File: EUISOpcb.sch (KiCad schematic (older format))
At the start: 13 parts

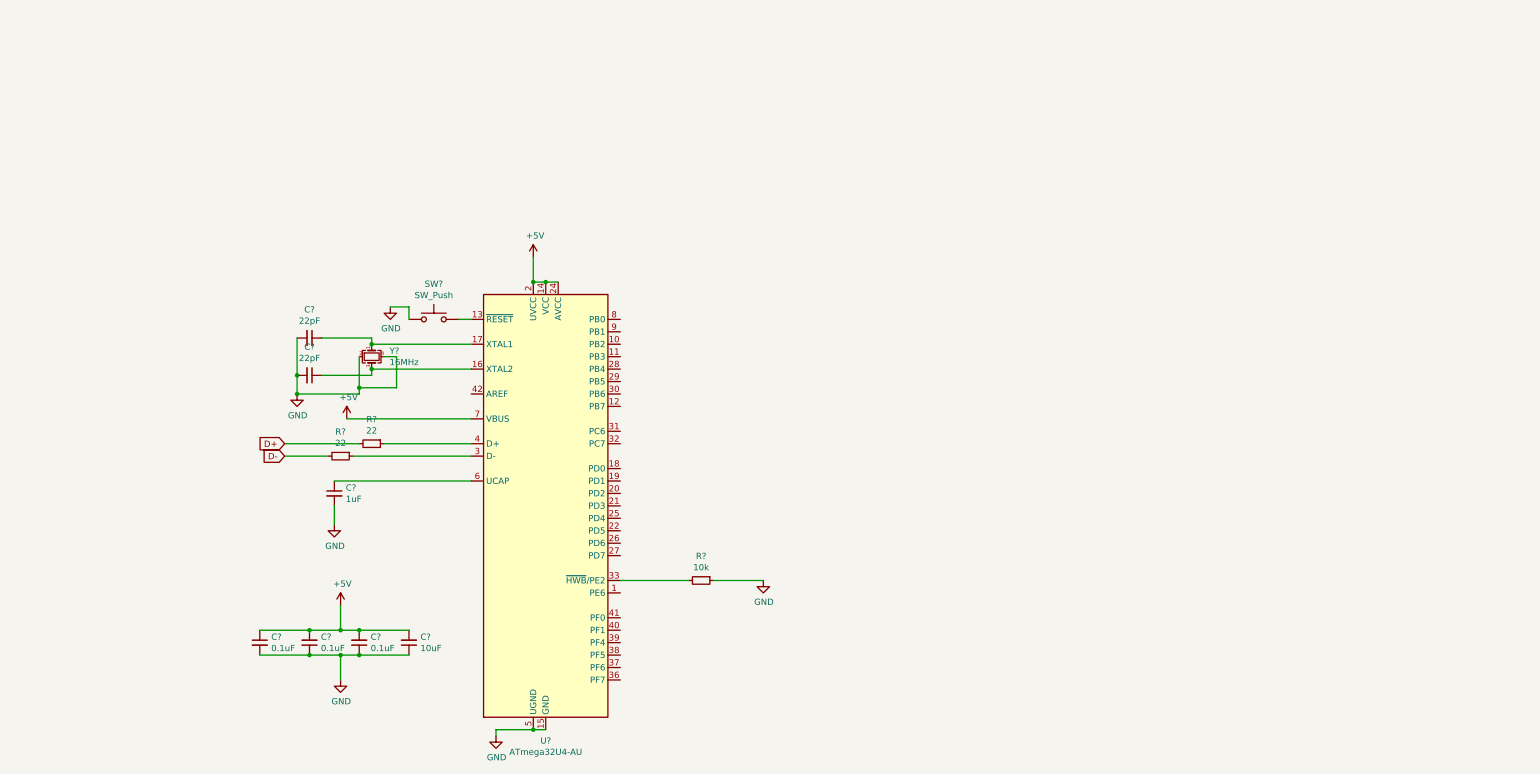
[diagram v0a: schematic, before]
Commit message: PCB Schematic/Traces Complete
Completed the PCB Schematic and traces!
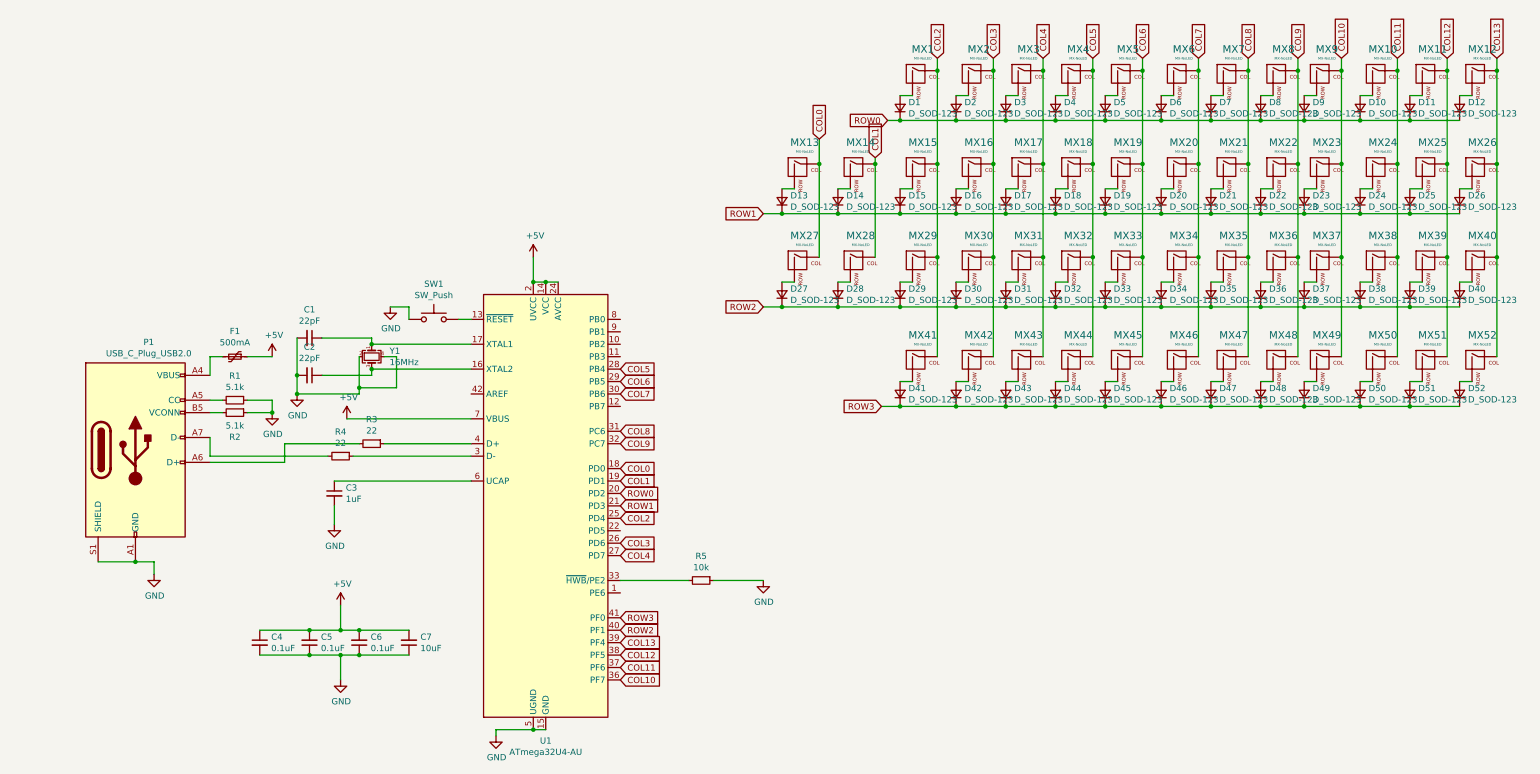
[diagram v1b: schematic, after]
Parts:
- added D1, D10, D11, D12, D13, D14, D15, D16, D17, D18, D19, D2, D20, D21, D22, D23, D24, D25, D26, D27, D28, D29, D3, D30, D31, D32, D33, D34, D35, D36, D37, D38, D39, D4, D40, D41, D42, D43, D44, D45, D46, D47, D48, D49, D5, D50, D51, D52, D6, D7, D8, D9: D_SOD-123, Diode_SMD:D_SOD-123, symbol Device:D_Small
- added F1: 500mA, Fuse:Fuse_1206_3216Metric, symbol Device:Polyfuse_Small
- added MX1, MX10, MX11, MX12, MX15, MX16, MX17, MX18, MX19, MX2, MX20, MX21, MX22, MX23, MX24, MX25, MX26, MX29, MX3, MX30, MX31, MX32, MX33, MX34, MX35, MX36, MX37, MX38, MX39, MX4, MX40, MX41, MX42, MX43, MX44, MX45, MX46, MX47, MX48, MX49, MX5, MX50, MX51, MX52, MX6, MX7, MX8, MX9: MX-NoLED, MX_Only:MXOnly-1U-NoLED, symbol MX_Alps_Hybrid:MX-NoLED
- added MX13, MX14, MX27, MX28: MX-NoLED, MX_Only:MXOnly-ISO, symbol MX_Alps_Hybrid:MX-NoLED
- added P1: USB_C_Plug_USB2.0, Connector_USB:USB_C_Receptacle_Amphenol_12401548E4-2A, symbol Connector:USB_C_Plug_USB2.0
- added R1, R2: 5.1k, Resistor_SMD:R_0805_2012Metric, symbol Device:R_Small
- C1, C2, C3, C4, C5, C6, C7: renamed from C?; footprint (none) -> Capacitor_SMD:C_0805_2012Metric
- R3, R4, R5: renamed from R?; footprint (none) -> Resistor_SMD:R_0805_2012Metric
- SW1: renamed from SW?; footprint (none) -> random-keyboard-parts:SKQG-1155865
- Y1: renamed from Y?; footprint (none) -> Crystal:Crystal_SMD_3225-4Pin_3.2x2.5mm
- gave numbers to parts that had none: 1
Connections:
- net +5V: now also F1.1
- net GND: now also P1.A1 (GND), P1.A12 (GND), P1.B1 (GND), P1.B12 (GND), P1.S1 (SHIELD), R1.1, R2.1
- net COL0: now reaches U1.18 (PD0)
- net COL0: now also MX13.1 (COL), MX27.1 (COL)
- net COL1: now reaches U1.19 (PD1)
- net COL1: now also MX14.1 (COL), MX28.1 (COL)
- net ROW0: now reaches U1.20 (PD2)
- net ROW0: now also D1.1 (K), D10.1 (K), D11.1 (K), D12.1 (K), D2.1 (K), D3.1 (K), D4.1 (K), D5.1 (K), D6.1 (K), D7.1 (K), D8.1 (K), D9.1 (K)
- net ROW1: now reaches U1.21 (PD3)
- net ROW1: now also D13.1 (K), D14.1 (K), D15.1 (K), D16.1 (K), D17.1 (K), D18.1 (K), D19.1 (K), D20.1 (K), D21.1 (K), D22.1 (K), D23.1 (K), D24.1 (K), D25.1 (K), D26.1 (K)
- net COL2: now reaches U1.25 (PD4)
- net COL2: now also MX1.1 (COL), MX15.1 (COL), MX29.1 (COL), MX41.1 (COL)
- net COL3: now reaches U1.26 (PD6)
- net COL3: now also MX16.1 (COL), MX2.1 (COL), MX30.1 (COL), MX42.1 (COL)
- net COL4: now reaches U1.27 (PD7)
- net COL4: now also MX17.1 (COL), MX3.1 (COL), MX31.1 (COL), MX43.1 (COL)
- net COL5: now reaches U1.28 (PB4)
- net COL5: now also MX18.1 (COL), MX32.1 (COL), MX4.1 (COL), MX44.1 (COL)
- net COL6: now reaches U1.29 (PB5)
- net COL6: now also MX19.1 (COL), MX33.1 (COL), MX45.1 (COL), MX5.1 (COL)
- net COL7: now reaches U1.30 (PB6)
- net COL7: now also MX20.1 (COL), MX34.1 (COL), MX46.1 (COL), MX6.1 (COL)
- net COL8: now reaches U1.31 (PC6)
- net COL8: now also MX21.1 (COL), MX35.1 (COL), MX47.1 (COL), MX7.1 (COL)
- net COL9: now reaches U1.32 (PC7)
- net COL9: now also MX22.1 (COL), MX36.1 (COL), MX48.1 (COL), MX8.1 (COL)
- net COL10: now reaches U1.36 (PF7)
- net COL10: now also MX23.1 (COL), MX37.1 (COL), MX49.1 (COL), MX9.1 (COL)
- net COL11: now reaches U1.37 (PF6)
- net COL11: now also MX10.1 (COL), MX24.1 (COL), MX38.1 (COL), MX50.1 (COL)
- net COL12: now reaches U1.38 (PF5)
- net COL12: now also MX11.1 (COL), MX25.1 (COL), MX39.1 (COL), MX51.1 (COL)
- net COL13: now reaches U1.39 (PF4)
- net COL13: now also MX12.1 (COL), MX26.1 (COL), MX40.1 (COL), MX52.1 (COL)
- net ROW2: now reaches U1.40 (PF1)
- net ROW2: now also D27.1 (K), D28.1 (K), D29.1 (K), D30.1 (K), D31.1 (K), D32.1 (K), D33.1 (K), D34.1 (K), D35.1 (K), D36.1 (K), D37.1 (K), D38.1 (K), D39.1 (K), D40.1 (K)
- net ROW3: now reaches U1.41 (PF0)
- net ROW3: now also D41.1 (K), D42.1 (K), D43.1 (K), D44.1 (K), D45.1 (K), D46.1 (K), D47.1 (K), D48.1 (K), D49.1 (K), D50.1 (K), D51.1 (K), D52.1 (K)
- net D+: no longer names the net of R3.2
- net D+: now also P1.A6 (D+)
- net D-: no longer names the net of R4.2
- net D-: now also P1.A7 (D-)
- new net: F1.2, P1.A4 (VBUS), P1.A9 (VBUS), P1.B4 (VBUS), P1.B9 (VBUS)
- new net: P1.A5 (CC), R1.2
- new net: P1.B5 (VCONN), R2.2
- new net: D1.2 (A), MX1.2 (ROW)
- new net: D2.2 (A), MX2.2 (ROW)
- new net: D3.2 (A), MX3.2 (ROW)
- new net: D4.2 (A), MX4.2 (ROW)
- new net: D5.2 (A), MX5.2 (ROW)
- new net: D6.2 (A), MX6.2 (ROW)
- new net: D7.2 (A), MX7.2 (ROW)
- new net: D8.2 (A), MX8.2 (ROW)
- new net: D9.2 (A), MX9.2 (ROW)
- new net: D10.2 (A), MX10.2 (ROW)
- new net: D11.2 (A), MX11.2 (ROW)
- new net: D12.2 (A), MX12.2 (ROW)
- new net: D15.2 (A), MX15.2 (ROW)
- new net: D16.2 (A), MX16.2 (ROW)
- new net: D17.2 (A), MX17.2 (ROW)
- new net: D18.2 (A), MX18.2 (ROW)
- new net: D19.2 (A), MX19.2 (ROW)
- new net: D20.2 (A), MX20.2 (ROW)
- new net: D21.2 (A), MX21.2 (ROW)
- new net: D22.2 (A), MX22.2 (ROW)
- new net: D23.2 (A), MX23.2 (ROW)
- new net: D24.2 (A), MX24.2 (ROW)
- new net: D25.2 (A), MX25.2 (ROW)
- new net: D26.2 (A), MX26.2 (ROW)
- new net: D29.2 (A), MX29.2 (ROW)
- new net: D30.2 (A), MX30.2 (ROW)
- new net: D31.2 (A), MX31.2 (ROW)
- new net: D32.2 (A), MX32.2 (ROW)
- new net: D33.2 (A), MX33.2 (ROW)
- new net: D34.2 (A), MX34.2 (ROW)
- new net: D35.2 (A), MX35.2 (ROW)
- new net: D36.2 (A), MX36.2 (ROW)
- new net: D37.2 (A), MX37.2 (ROW)
- new net: D38.2 (A), MX38.2 (ROW)
- new net: D39.2 (A), MX39.2 (ROW)
- new net: D40.2 (A), MX40.2 (ROW)
- new net: D41.2 (A), MX41.2 (ROW)
- new net: D42.2 (A), MX42.2 (ROW)
- new net: D43.2 (A), MX43.2 (ROW)
- new net: D44.2 (A), MX44.2 (ROW)
- new net: D45.2 (A), MX45.2 (ROW)
- new net: D46.2 (A), MX46.2 (ROW)
- new net: D47.2 (A), MX47.2 (ROW)
- new net: D48.2 (A), MX48.2 (ROW)
- new net: D49.2 (A), MX49.2 (ROW)
- new net: D50.2 (A), MX50.2 (ROW)
- new net: D51.2 (A), MX51.2 (ROW)
- new net: D52.2 (A), MX52.2 (ROW)
- new net: D13.2 (A), MX13.2 (ROW)
- new net: D14.2 (A), MX14.2 (ROW)
- new net: D27.2 (A), MX27.2 (ROW)
- new net: D28.2 (A), MX28.2 (ROW)

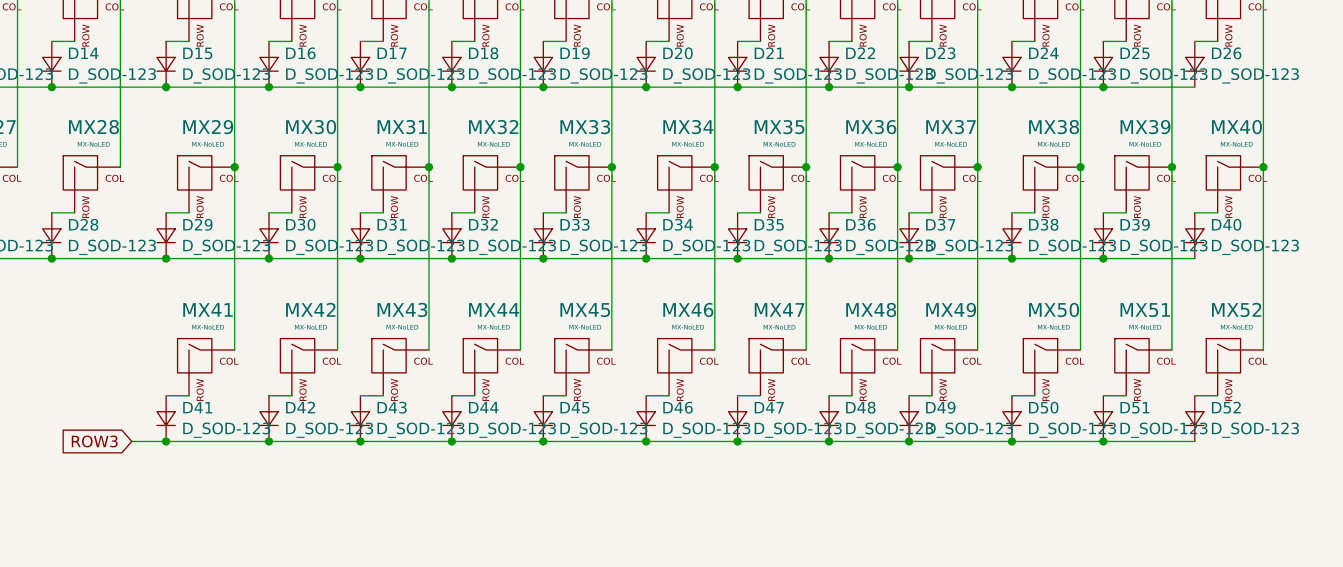
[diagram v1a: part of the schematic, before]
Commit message: Completed PCB
Completed the PCB by adding 7u Support and new decorations
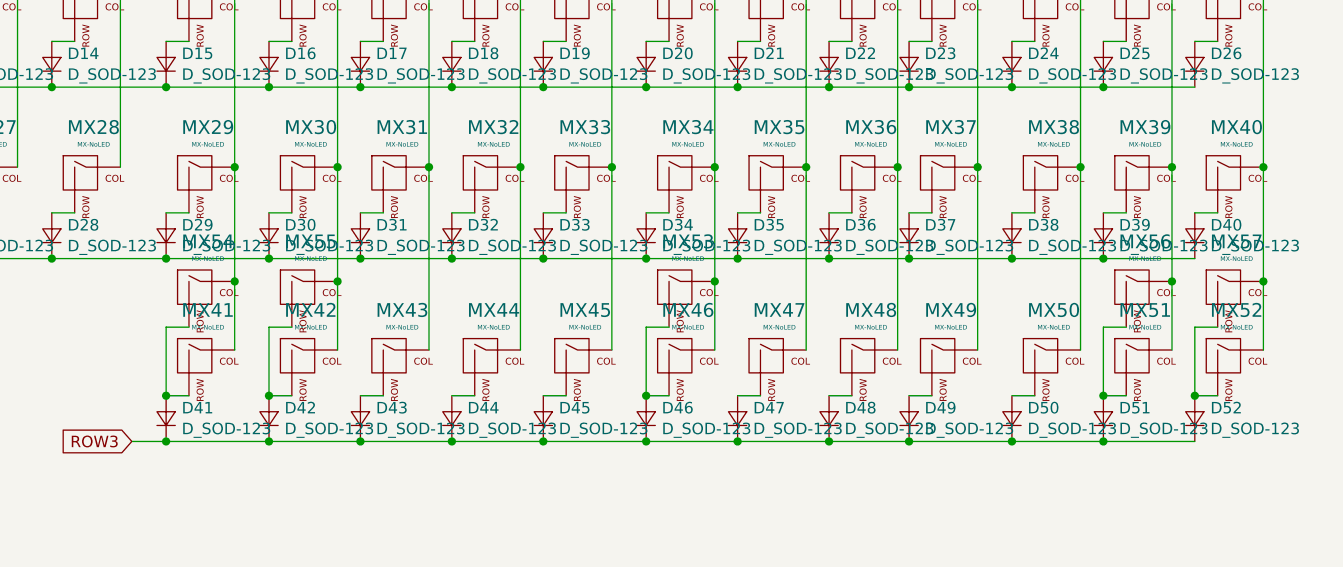
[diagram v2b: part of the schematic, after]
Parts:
- added MX53: MX-NoLED, MX_Only:MXOnly-7U-ReversedStabilizers-NoLED, symbol MX_Alps_Hybrid:MX-NoLED
- added MX54, MX55, MX56, MX57: MX-NoLED, MX_Only:MXOnly-1.25U-NoLED, symbol MX_Alps_Hybrid:MX-NoLED
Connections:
- net COL12: now also MX56.1 (COL)
- net COL13: now also MX57.1 (COL)
- net COL2: now also MX54.1 (COL)
- net COL3: now also MX55.1 (COL)
- net COL7: now also MX53.1 (COL)
- net at D41.2 (A), MX41.2 (ROW): now also MX54.2 (ROW)
- net at D42.2 (A), MX42.2 (ROW): now also MX55.2 (ROW)
- net at D46.2 (A), MX46.2 (ROW): now also MX53.2 (ROW)
- net at D51.2 (A), MX51.2 (ROW): now also MX56.2 (ROW)
- net at D52.2 (A), MX52.2 (ROW): now also MX57.2 (ROW)
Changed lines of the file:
@@
 	10200 2550 10200 1800
 Wire Wire Line
-	10600 3350 10600 2550
+	10600 3350 10600 3050
 Connection ~ 10600 1800
 Wire Wire Line
@@
 	10600 2550 10600 1800
 Wire Wire Line
-	11000 3350 11000 2550
+	11000 3350 11000 3050
 Connection ~ 11000 1800
 Wire Wire Line
@@
 	9000 2550 9000 1800
 Wire Wire Line
-	8600 3350 8600 2550
+	8600 3350 8600 3050
 Connection ~ 8600 1800
 Wire Wire Line
@@
 	7350 2550 7350 1800
 Wire Wire Line
-	6950 3350 6950 2550
+	6950 3350 6950 3050
 Connection ~ 6950 1800
 Wire Wire Line
@@
 	6950 2550 6950 1800
 Wire Wire Line
-	6500 3350 6500 2550
+	6500 3350 6500 3050
 Connection ~ 6500 1800
 Wire Wire Line
@@
 Text GLabel 3950 5750 2    50   Input ~ 0
 COL12
+$Comp
+L MX_Alps_Hybrid:MX-NoLED MX53
+U 1 1 5E322DED
+P 8450 3100
+F 0 "MX53" H 8483 3323 60  0000 C CNN
+F 1 "MX-NoLED" H 8483 3249 20  0000 C CNN
+F 2 "MX_Only:MXOnly-7U-ReversedStabilizers-NoLED" H 7825 3075 60  0001 C CNN
+F 3 "" H 7825 3075 60  0001 C CNN
+	1    8450 3100
+	1    0    0    -1
+$EndComp
+Connection ~ 8600 3050
+Wire Wire Line
+	8600 3050 8600 2550
+Wire Wire Line
+	8400 3250 8300 3250
+Wire Wire Line
+	8300 3250 8300 3550
+Connection ~ 8300 3550
+$Comp
+L MX_Alps_Hybrid:MX-NoLED MX56
+U 1 1 5E36CE5A
+P 10450 3100
+F 0 "MX56" H 10483 3323 60  0000 C CNN
+F 1 "MX-NoLED" H 10483 3249 20  0000 C CNN
+F 2 "MX_Only:MXOnly-1.25U-NoLED" H 9825 3075 60  0001 C CNN
+F 3 "" H 9825 3075 60  0001 C CNN
+	1    10450 3100
+	1    0    0    -1
+$EndComp
+Connection ~ 10600 3050
+Wire Wire Line
+	10600 3050 10600 2550
+$Comp
+L MX_Alps_Hybrid:MX-NoLED MX57
+U 1 1 5E36F3FF
+P 10850 3100
+F 0 "MX57" H 10883 3323 60  0000 C CNN
+F 1 "MX-NoLED" H 10883 3249 20  0000 C CNN
+F 2 "MX_Only:MXOnly-1.25U-NoLED" H 10225 3075 60  0001 C CNN
+F 3 "" H 10225 3075 60  0001 C CNN
+	1    10850 3100
+	1    0    0    -1
+$EndComp
+Connection ~ 11000 3050
+Wire Wire Line
+	11000 3050 11000 2550
+Wire Wire Line
+	10800 3250 10700 3250
+Wire Wire Line
+	10700 3250 10700 3550
+Connection ~ 10700 3550
+Wire Wire Line
+	10400 3250 10300 3250
+Wire Wire Line
+	10300 3250 10300 3550
+Connection ~ 10300 3550
+$Comp
+L MX_Alps_Hybrid:MX-NoLED MX54
+U 1 1 5E38C282
+P 6350 3100
+F 0 "MX54" H 6383 3323 60  0000 C CNN
+F 1 "MX-NoLED" H 6383 3249 20  0000 C CNN
+F 2 "MX_Only:MXOnly-1.25U-NoLED" H 5725 3075 60  0001 C CNN
+F 3 "" H 5725 3075 60  0001 C CNN
+	1    6350 3100
+	1    0    0    -1
+$EndComp
+Connection ~ 6500 3050
+Wire Wire Line
+	6500 3050 6500 2550
+$Comp
+L MX_Alps_Hybrid:MX-NoLED MX55
+U 1 1 5E38D9E3
+P 6800 3100
+F 0 "MX55" H 6833 3323 60  0000 C CNN
+F 1 "MX-NoLED" H 6833 3249 20  0000 C CNN
+F 2 "MX_Only:MXOnly-1.25U-NoLED" H 6175 3075 60  0001 C CNN
+F 3 "" H 6175 3075 60  0001 C CNN
+	1    6800 3100
+	1    0    0    -1
+$EndComp
+Connection ~ 6950 3050
+Wire Wire Line
+	6950 3050 6950 2550
+Wire Wire Line
+	6750 3250 6650 3250
+Wire Wire Line
+	6650 3250 6650 3550
+Connection ~ 6650 3550
+Wire Wire Line
+	6300 3250 6200 3250
+Wire Wire Line
+	6200 3250 6200 3550
+Connection ~ 6200 3550
 $EndSCHEMATC

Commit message: Idk what I did this time
But it was definitely something, it is complete though
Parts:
- removed P1: USB_C_Plug_USB2.0, Connector_USB:USB_C_Receptacle_Amphenol_12401548E4-2A, symbol Connector:USB_C_Plug_USB2.0
- added J1: USB_C_Receptacle_USB2.0, Connector_USB:USB_C_Receptacle_HRO_TYPE-C-31-M-12, symbol Connector:USB_C_Receptacle_USB2.0
- R3, R4: value 22 -> 22 Ohm
- U1: LCSC (none) -> C44854
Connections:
- net GND: now also J1.A1 (GND), J1.A12 (GND), J1.B1 (GND), J1.B12 (GND)
- net at R3.2: now also J1.A6 (D+), J1.B6 (D+)
- net at R4.2: now also J1.A7 (D-), J1.B7 (D-)
- net at F1.2: now also J1.A4 (VBUS), J1.A9 (VBUS), J1.B4 (VBUS), J1.B9 (VBUS)
- net at R1.2: now also J1.A5 (CC1)
- net at R2.2: now also J1.B5 (CC2)
- no-connect marks 0 -> 3
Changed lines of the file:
@@
 F 2 "Package_QFP:TQFP-44_10x10mm_P0.8mm" H 3350 4550 50  0001 C CIN
 F 3 "http://ww1.microchip.com/downloads/en/DeviceDoc/Atmel-7766-8-bit-AVR-ATmega16U4-32U4_Datasheet.pdf" H 3350 4550 50  0001 C CNN
+F 4 "C44854" H 3350 4550 50  0001 C CNN "LCSC"
 	1    3350 4550
 	1    0    0    -1
@@
 P 1950 4050
 F 0 "R3" V 1754 4050 50  0000 C CNN
-F 1 "22" V 1845 4050 50  0000 C CNN
+F 1 "22 Ohm" V 1845 4050 50  0000 C CNN
 F 2 "Resistor_SMD:R_0805_2012Metric" H 1950 4050 50  0001 C CNN
 F 3 "~" H 1950 4050 50  0001 C CNN
@@
 P 1700 4150
 F 0 "R4" V 1504 4150 50  0000 C CNN
-F 1 "22" V 1595 4150 50  0000 C CNN
+F 1 "22 Ohm" V 1595 4150 50  0000 C CNN
 F 2 "Resistor_SMD:R_0805_2012Metric" H 1700 4150 50  0001 C CNN
 F 3 "~" H 1700 4150 50  0001 C CNN
@@
 Wire Wire Line
 	2250 2950 2250 3050
-$Comp
-L Connector:USB_C_Plug_USB2.0 P1
-U 1 1 5E018D19
-P 50 4100
-F 0 "P1" H 157 4967 50  0000 C CNN
-F 1 "USB_C_Plug_USB2.0" H 157 4876 50  0000 C CNN
-F 2 "Connector_USB:USB_C_Receptacle_Amphenol_12401548E4-2A" H 200 4100 50  0001 C CNN
-F 3 "https://www.usb.org/sites/default/files/documents/usb_type-c.zip" H 200 4100 50  0001 C CNN
-	1    50   4100
-	1    0    0    -1
-$EndComp
 Wire Wire Line
 	1850 4050 1250 4050
@@
 Wire Wire Line
 	1250 4050 1250 4200
-Wire Wire Line
-	1250 4200 650  4200
 $Comp
 L Device:R_Small R1
@@
 	0    1    1    0
 $EndComp
-Wire Wire Line
-	650  3700 750  3700
-Wire Wire Line
-	750  3800 650  3800
 $Comp
 L power:GND #PWR05
@@
 	1150 3700 1150 3800
 Connection ~ 1150 3800
-Wire Wire Line
-	-250 5000 50   5000
 $Comp
 L power:GND #PWR08
 U 1 1 5E03DFBE
-P 200 5100
-F 0 "#PWR08" H 200 4850 50  0001 C CNN
-F 1 "GND" H 205 4927 50  0000 C CNN
-F 2 "" H 200 5100 50  0001 C CNN
-F 3 "" H 200 5100 50  0001 C CNN
-	1    200  5100
-	1    0    0    -1
-$EndComp
-Wire Wire Line
-	50   5000 200  5000
-Wire Wire Line
-	200  5000 200  5100
-Connection ~ 50   5000
+P -350 5100
+F 0 "#PWR08" H -350 4850 50  0001 C CNN
+F 1 "GND" H -345 4927 50  0000 C CNN
+F 2 "" H -350 5100 50  0001 C CNN
+F 3 "" H -350 5100 50  0001 C CNN
+	1    -350 5100
+	1    0    0    -1
+$EndComp
+Wire Wire Line
+	-350 5000 -350 5100
 $Comp
 L Device:Polyfuse_Small F1
@@
 	6200 3250 6200 3550
 Connection ~ 6200 3550
+$Comp
+L Connector:USB_C_Receptacle_USB2.0 J1
+U 1 1 5E822995
+P -500 4100
+F 0 "J1" H -393 4967 50  0000 C CNN
+F 1 "USB_C_Receptacle_USB2.0" H -393 4876 50  0000 C CNN
+F 2 "Connector_USB:USB_C_Receptacle_HRO_TYPE-C-31-M-12" H -350 4100 50  0001 C CNN
+F 3 "https://www.usb.org/sites/default/files/documents/usb_type-c.zip" H -350 4100 50  0001 C CNN
+	1    -500 4100
+	1    0    0    -1
+$EndComp
+Wire Wire Line
+	-500 5000 -350 5000
+Wire Wire Line
+	100  3700 750  3700
+Wire Wire Line
+	100  3800 750  3800
+Wire Wire Line
+	100  4100 200  4100
+Wire Wire Line
+	200  4100 200  4000
+Wire Wire Line
+	100  4000 200  4000
+Connection ~ 200  4000
+Wire Wire Line
+	200  4000 650  4000
+Wire Wire Line
+	100  4200 250  4200
+Wire Wire Line
+	100  4300 250  4300
+Wire Wire Line
+	250  4300 250  4200
+Connection ~ 250  4200
+Wire Wire Line
+	250  4200 1250 4200
+Wire Wire Line
+	100  3500 650  3500
+NoConn ~ 100  4600
+NoConn ~ 100  4700
+NoConn ~ -800 5000
 $EndSCHEMATC
